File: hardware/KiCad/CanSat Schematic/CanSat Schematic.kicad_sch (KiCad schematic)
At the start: 19 parts, among them J5 JST-PH 1x2, J6 JST-PH 1x3 Servo 1, J7 JST-PH 1x3 Servo 2, U1 ZED-X20P, U2 Teensy4.0, U3 BNO085, U4 Pololu 2597, U5 CORE1262-LF, U6 D24V10F3, U7 D24V22F5, U9 BMP280

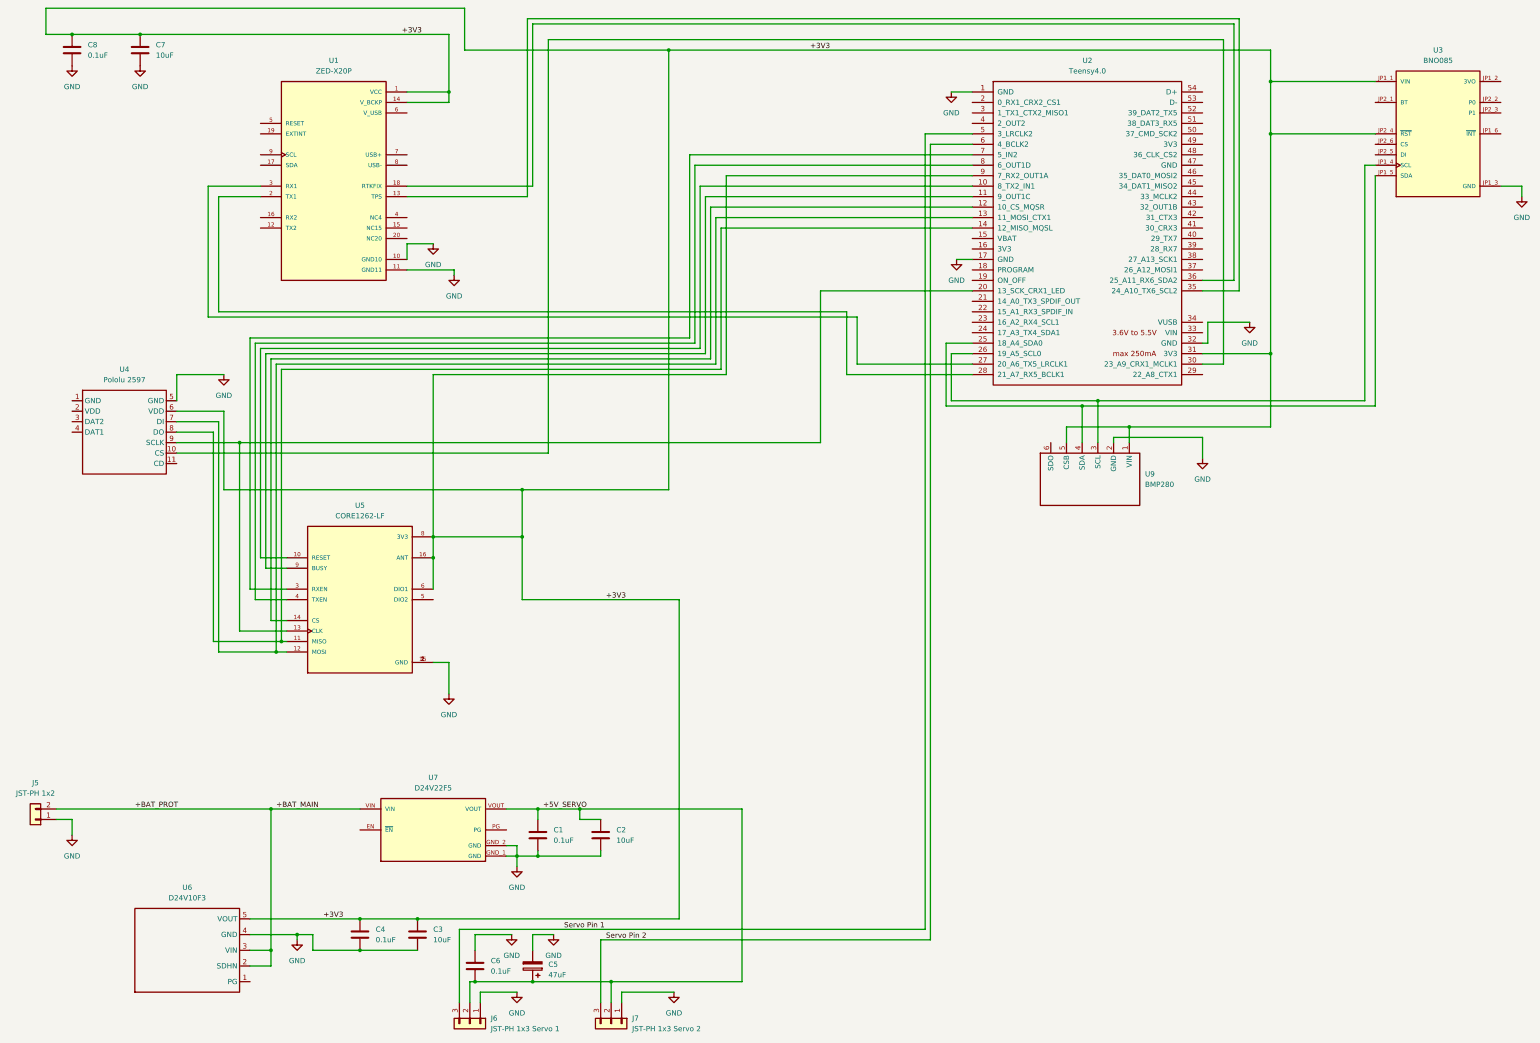
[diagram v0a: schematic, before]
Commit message: Added 3D models for each PCB
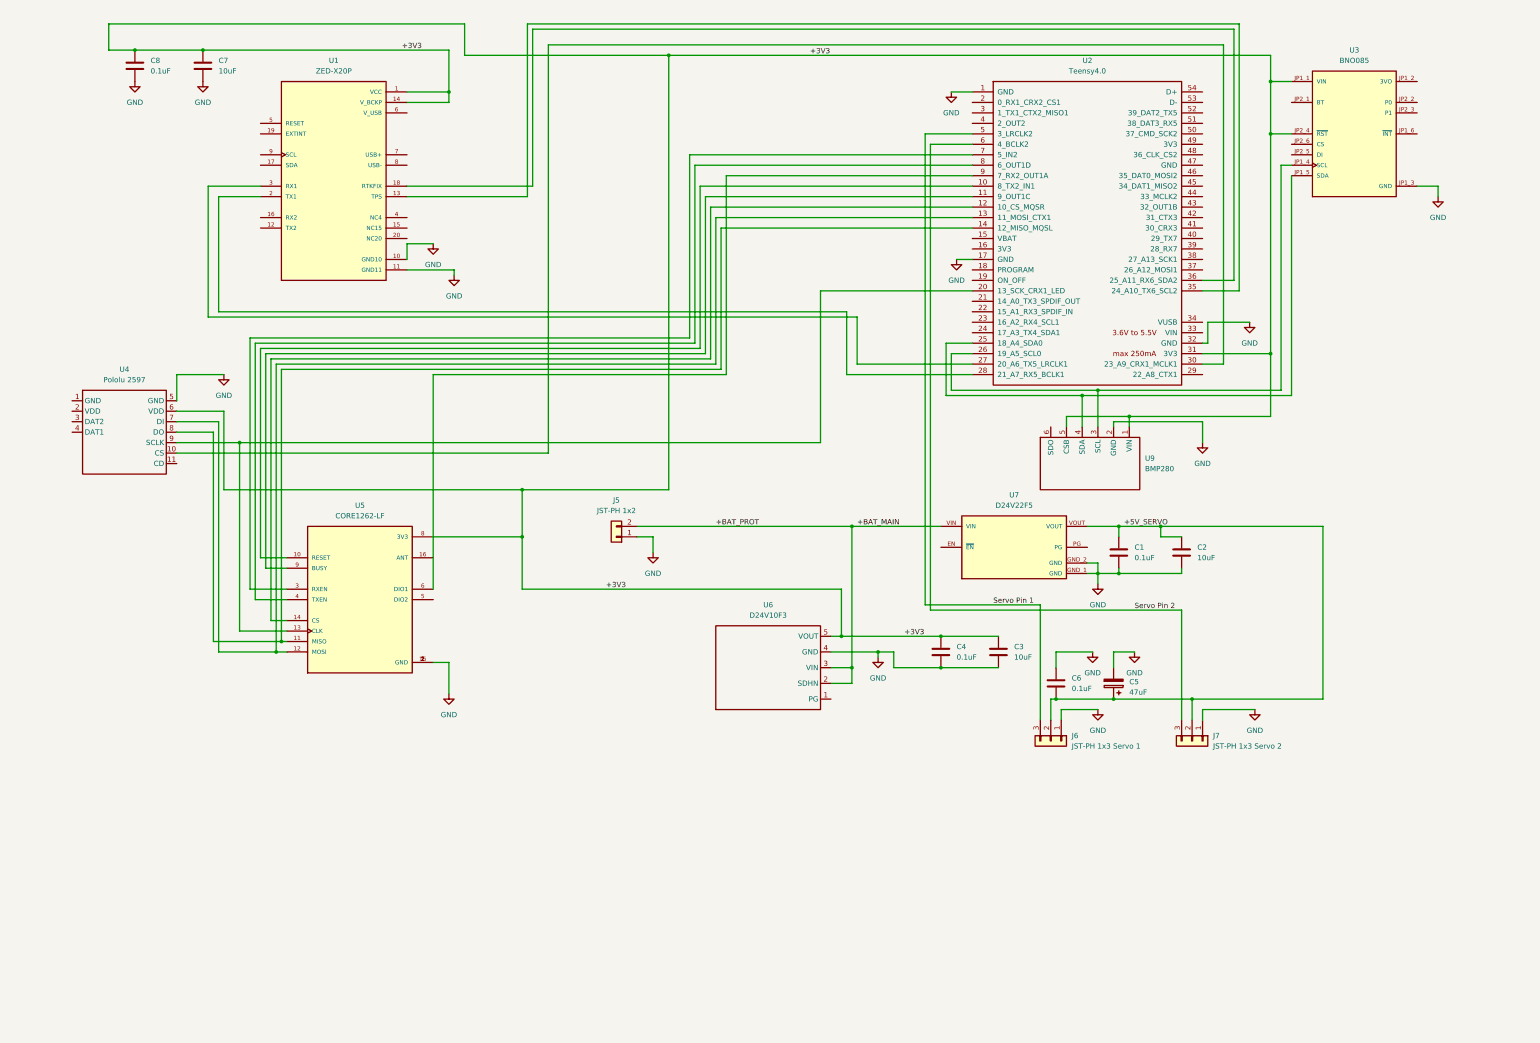
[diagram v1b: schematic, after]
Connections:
- net +3V3: no longer U2.9 (7_RX2_OUT1A), U5.16 (ANT), U5.6 (DIO1)
- new net: U2.9 (7_RX2_OUT1A), U5.6 (DIO1)
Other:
- moved on the sheet: C1, C2, C3, C4, C5, C6, C7, C8, J5, J6, J7, U3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
